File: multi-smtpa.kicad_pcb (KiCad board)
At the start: 4 copper layers, 100 x 100 mm, 121 parts, among them J1 Screw_Terminal_01x02, J10 Conn_Coaxial, J11 J SMTPA, J12 J SMTPA, J13 Conn_Coaxial, J14 J SMTPA, J15 Conn_Coaxial, J16 J SMTPA, J17 J SMTPA, J18 Conn_Coaxial, J19 Conn_Coaxial, J2 J SMTPA, J20 J SMTPA, J21 Conn_Coaxial, J3 J SMTPA, J4 J SMTPA, J5 Conn_Coaxial, J6 J SMTPA, J7 J SMTPA, J8 Conn_Coaxial, J9 Conn_Coaxial, U1 LM317L_SO8, U2 LM317L_SO8, U3 LM317L_SO8, U4 LM317L_SO8, U5 ADL5610, U6 LM317L_SO8, U7 LM317L_SO8, U8 LM317L_SO8

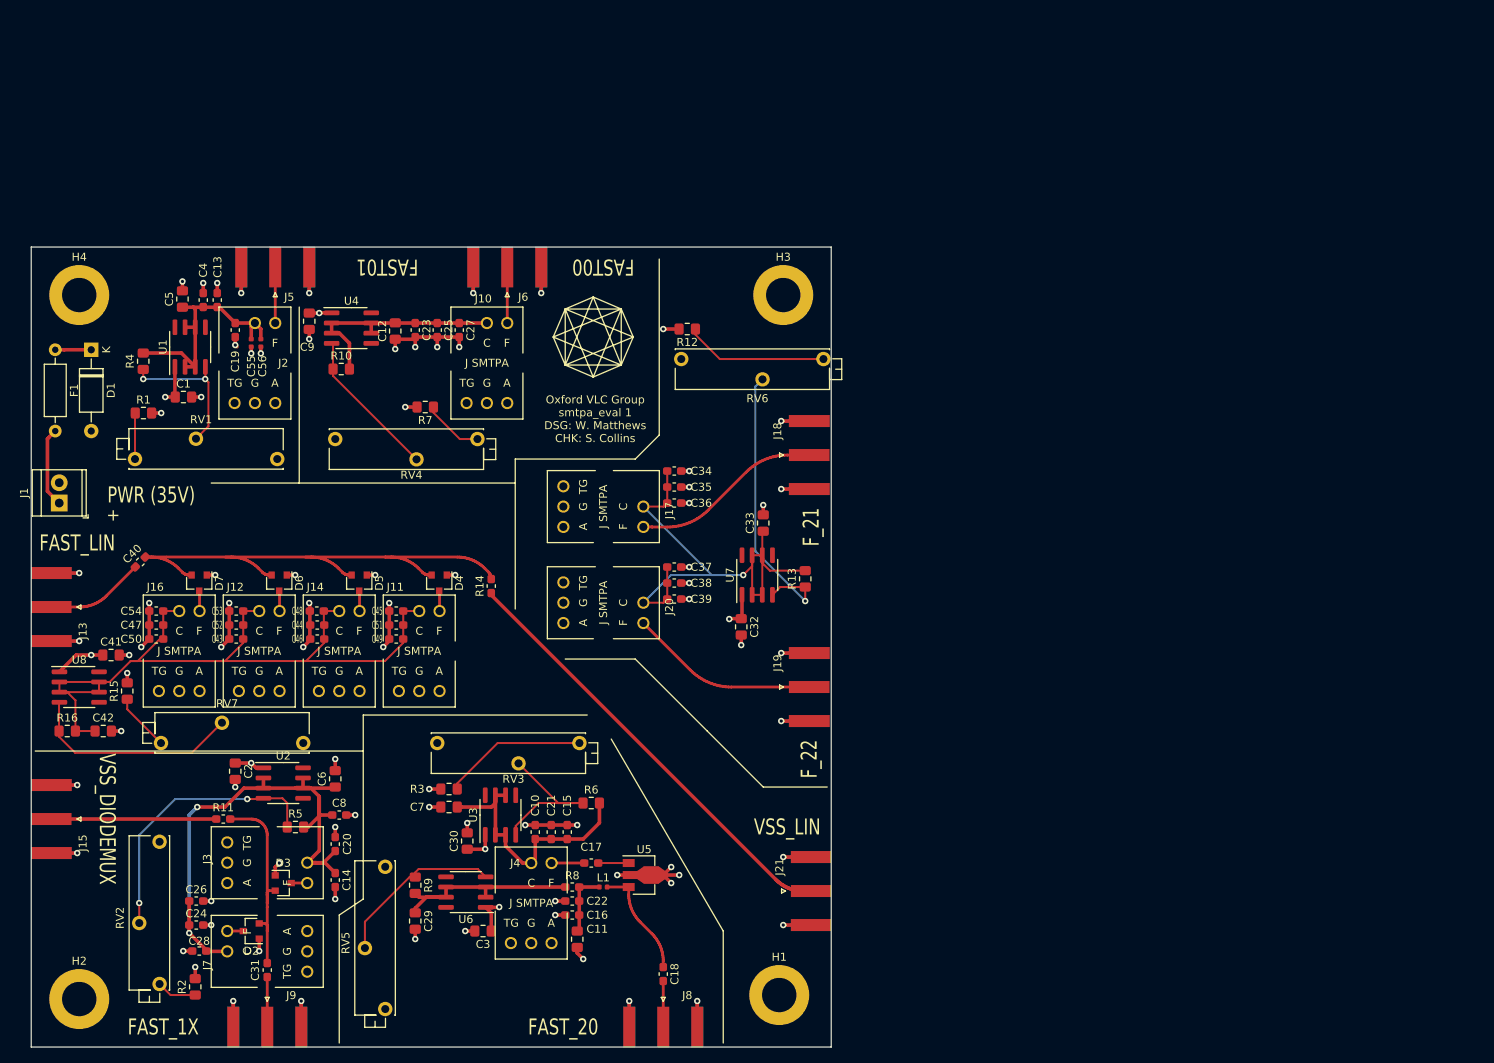
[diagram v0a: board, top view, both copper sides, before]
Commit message: added another experiment, testpoints, fiducials
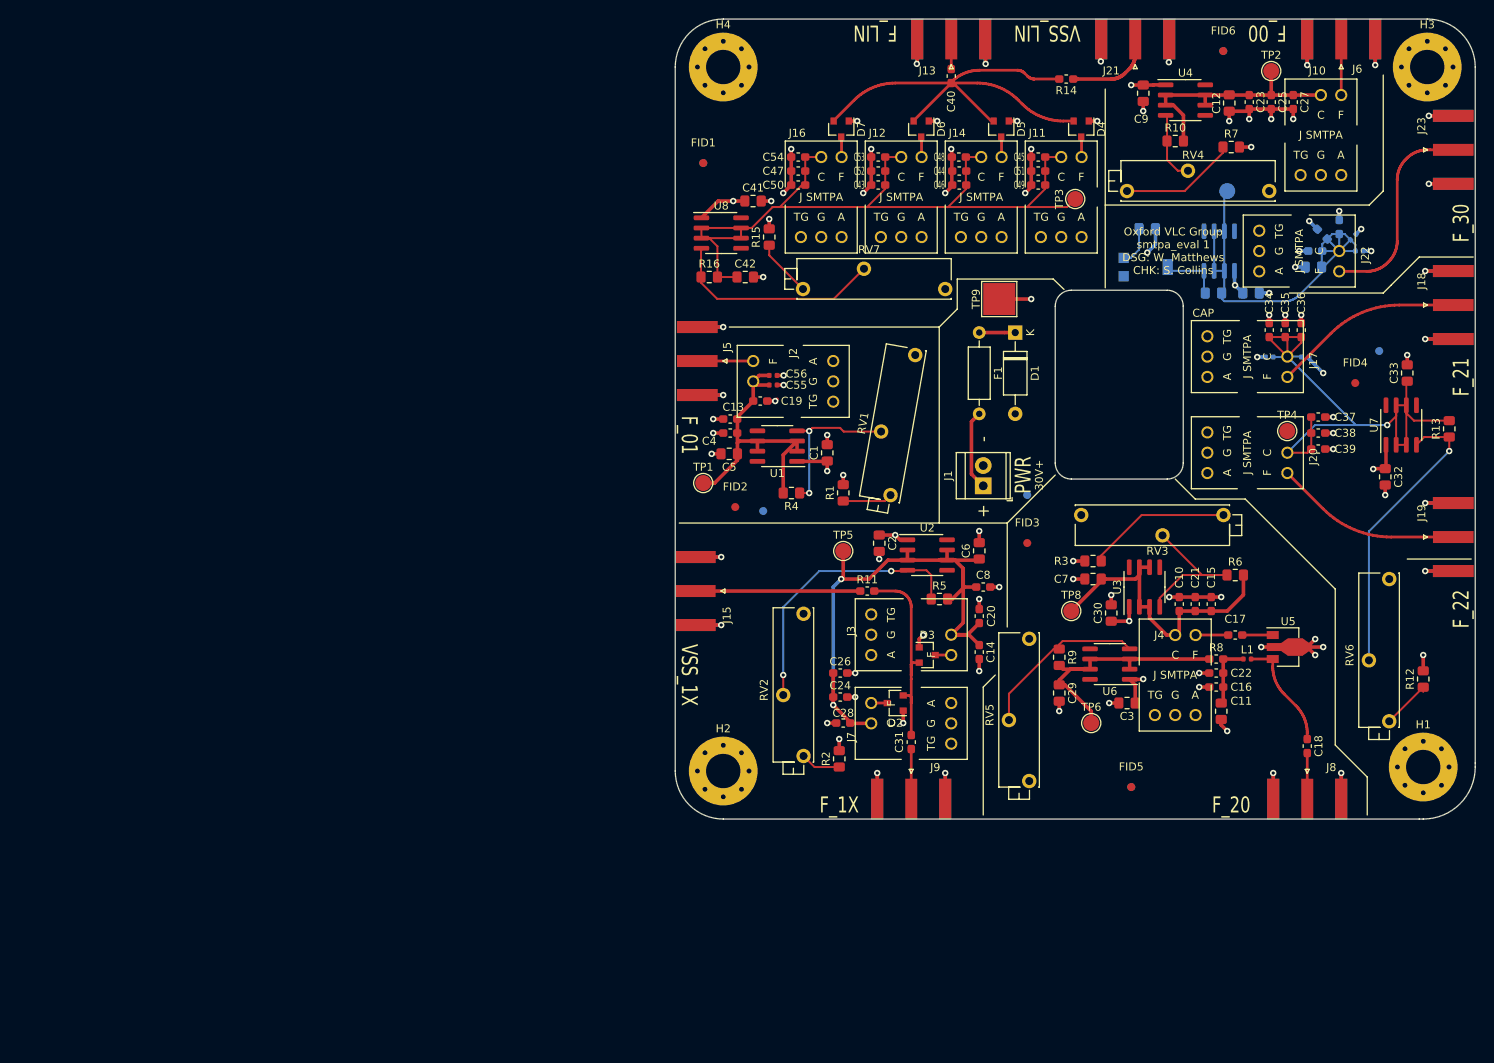
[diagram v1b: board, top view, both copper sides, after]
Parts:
- added C57: 100p, Capacitor_SMD:C_0402_1005Metric, B.Cu at (178.8, 92.2)
- added C58: 10p, Capacitor_SMD:C_0402_1005Metric, B.Cu at (174.3, 92.2)
- added C59: 100n, Capacitor_SMD:C_0603_1608Metric_Pad1.05x0.95mm_HandSolder, B.Cu at (180.0, 79.0)
- added C60: 0.1u, Capacitor_SMD:C_0805_2012Metric_Pad1.15x1.40mm_HandSolder, B.Cu at (172.0, 84.2)
- added C61: 10n, Capacitor_SMD:C_0603_1608Metric_Pad1.05x0.95mm_HandSolder, B.Cu at (183.0, 76.0)
- added C62: 1n, Capacitor_SMD:C_0603_1608Metric_Pad1.05x0.95mm_HandSolder, B.Cu at (180.9, 76.9)
- added C63: 100p, Capacitor_SMD:C_0402_1005Metric, B.Cu at (184.8, 77.2)
- added C64: 1u, Capacitor_SMD:C_0805_2012Metric_Pad1.15x1.40mm_HandSolder, B.Cu at (179.8, 81.0)
- added C65: 10p, Capacitor_SMD:C_0402_1005Metric, B.Cu at (185.5, 79.0)
- added FID1: Fiducial, Fiducial:Fiducial_1mm_Mask3mm, F.Cu at (103.5, 68.0)
- added FID10: Fiducial, Fiducial:Fiducial_1mm_Mask3mm, B.Cu at (188.0, 91.5)
- added FID11: Fiducial, Fiducial:Fiducial_1mm_Mask3mm, B.Cu at (157.0, 146.0)
- added FID12: Fiducial, Fiducial:Fiducial_1mm_Mask3mm, B.Cu at (168.5, 54.0)
- added FID2: Fiducial, Fiducial:Fiducial_1mm_Mask3mm, F.Cu at (107.5, 111.0)
- added FID3: Fiducial, Fiducial:Fiducial_1mm_Mask3mm, F.Cu at (144.0, 115.5)
- added FID4: Fiducial, Fiducial:Fiducial_1mm_Mask3mm, F.Cu at (185.0, 95.5)
- added FID5: Fiducial, Fiducial:Fiducial_1mm_Mask3mm, F.Cu at (157.0, 146.0)
- added FID6: Fiducial, Fiducial:Fiducial_1mm_Mask3mm, F.Cu at (168.5, 54.0)
- added FID7: Fiducial, Fiducial:Fiducial_1mm_Mask3mm, B.Cu at (103.5, 68.0)
- added FID8: Fiducial, Fiducial:Fiducial_1mm_Mask3mm, B.Cu at (111.0, 111.5)
- added FID9: Fiducial, Fiducial:Fiducial_1mm_Mask3mm, B.Cu at (144.0, 109.5)
- added J22: J SMTPA, footprints:SMTPA J30035, F.Cu at (178.0, 79.0)
- added J23: Conn_Coaxial, Connector_Coaxial:SMA_Amphenol_132289_EdgeMount, F.Cu at (197.2, 66.3)
- added R17: 1K0, Resistor_SMD:R_0805_2012Metric_Pad1.15x1.40mm_HandSolder, B.Cu at (159.0, 76.2)
- added R18: 240R, Resistor_SMD:R_0805_2012Metric_Pad1.15x1.40mm_HandSolder, B.Cu at (167.3, 84.2)
- added RV8: R_POT_TRIM, Potentiometer_SMD:Potentiometer_Bourns_3314G_Vertical, B.Cu at (158.8, 81.0)
- added TP1: TestPoint, TestPoint:TestPoint_Pad_D2.0mm, F.Cu at (103.5, 108.0)
- added TP2: TestPoint, TestPoint:TestPoint_Pad_D2.0mm, F.Cu at (174.5, 56.5)
- added TP3: TestPoint, TestPoint:TestPoint_Pad_D2.0mm, F.Cu at (150.0, 72.5)
- added TP4: TestPoint, TestPoint:TestPoint_Pad_D2.0mm, F.Cu at (176.5, 101.5)
- added TP5: TestPoint, TestPoint:TestPoint_Pad_D2.0mm, F.Cu at (121.0, 116.5)
- added TP6: TestPoint, TestPoint:TestPoint_Pad_D2.0mm, F.Cu at (152.0, 138.0)
- added TP7: TestPoint, TestPoint:TestPoint_Pad_D2.0mm, B.Cu at (169.0, 71.5)
- added TP8: TestPoint, TestPoint:TestPoint_Pad_D2.0mm, F.Cu at (149.5, 124.0)
- added TP9: TestPoint, TestPoint:TestPoint_Pad_4.0x4.0mm, F.Cu at (140.5, 85.0)
- added U9: LM317L_SO8, Package_SO:SOIC-8_3.9x4.9mm_P1.27mm, B.Cu at (168.0, 79.0)
- H1, H2, H3, H4: footprint MountingHole:MountingHole_4.3mm_M4_DIN965_Pad -> MountingHole:MountingHole_4.3mm_M4_Pad_Via
- moved J13 133.0 mm to (134.5, 52.5), turned to 90 degrees
- moved RV4 120.8 mm to (174.2, 71.5), turned to 0 degrees
- moved C40 118.2 mm to (134.5, 57.1), turned to 270 degrees
- moved D1 115.5 mm to (142.5, 89.2)
- moved F1 115.5 mm to (138.0, 89.2)
- moved J1 115.5 mm to (138.5, 108.3)
- moved J21 113.9 mm to (157.5, 52.5), turned to 90 degrees
- moved J6 108.1 mm to (180.7, 64.5)
- moved C12 108.1 mm to (169.2, 60.5)
- moved C23 108.1 mm to (171.8, 60.4)
- moved C25 108.1 mm to (174.5, 60.4)
- moved C27 108.1 mm to (177.2, 60.4)
- moved C9 108.1 mm to (158.5, 59.3)
- moved J10 108.1 mm to (183.2, 52.5)
- moved R10 108.1 mm to (162.5, 65.2)
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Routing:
- net /VDC_30: track 0.00 -> 58.3 mm
- net /VssFast_lin: track 55.4 -> 11.4 mm
- net GND: track 231.8 -> 259.3 mm, vias 81 -> 94
- net /Fast_30: track 0.00 -> 26.2 mm
- net Net-(R12-Pad1): track 18.0 -> 6.59 mm
- net Net-(R10-Pad1): track 18.9 -> 8.57 mm
- net /VDC_21: track 70.9 -> 80.4 mm
- net /Fast_lin: track 70.3 -> 61.4 mm
- net /CFast_lin: track 12.4 -> 4.10 mm
- net Net-(R18-Pad1): track 0.00 -> 7.58 mm
- net Net-(R7-Pad1): track 7.57 -> 14.7 mm
- net /TEEBFast_20: track 26.5 -> 33.3 mm
- net /VDC_lin: track 99.8 -> 106.2 mm
- net /VDC_00: track 31.7 -> 38.0 mm
- net /VDC_20: track 33.5 -> 39.0 mm
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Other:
- outline, holes or cut-outs redrawn
- board text added: "-"
- board text added: "30V+"
- board text added: "CAP"
- board text added: "F_00"
- board text added: "F_01"
- board text added: "F_1X"
- board text added: "F_20"
- board text added: "F_30"
- board text added: "F_LIN"
- board text added: "Oxford VLC"
- board text added: "PWR"
- board text added: "VSS_1X"
- board text removed: "FAST00"
- board text removed: "FAST01"
- board text removed: "FAST_1X"
- board text removed: "FAST_20"
- board text removed: "FAST_LIN"
- board text removed: "PWR (35V)"
- board text removed: "VSS_DIODEMUX"
